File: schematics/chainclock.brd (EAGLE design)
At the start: 72 x 39.5 mm, 19 parts, among them SW1 ROTARTY_ENCODER

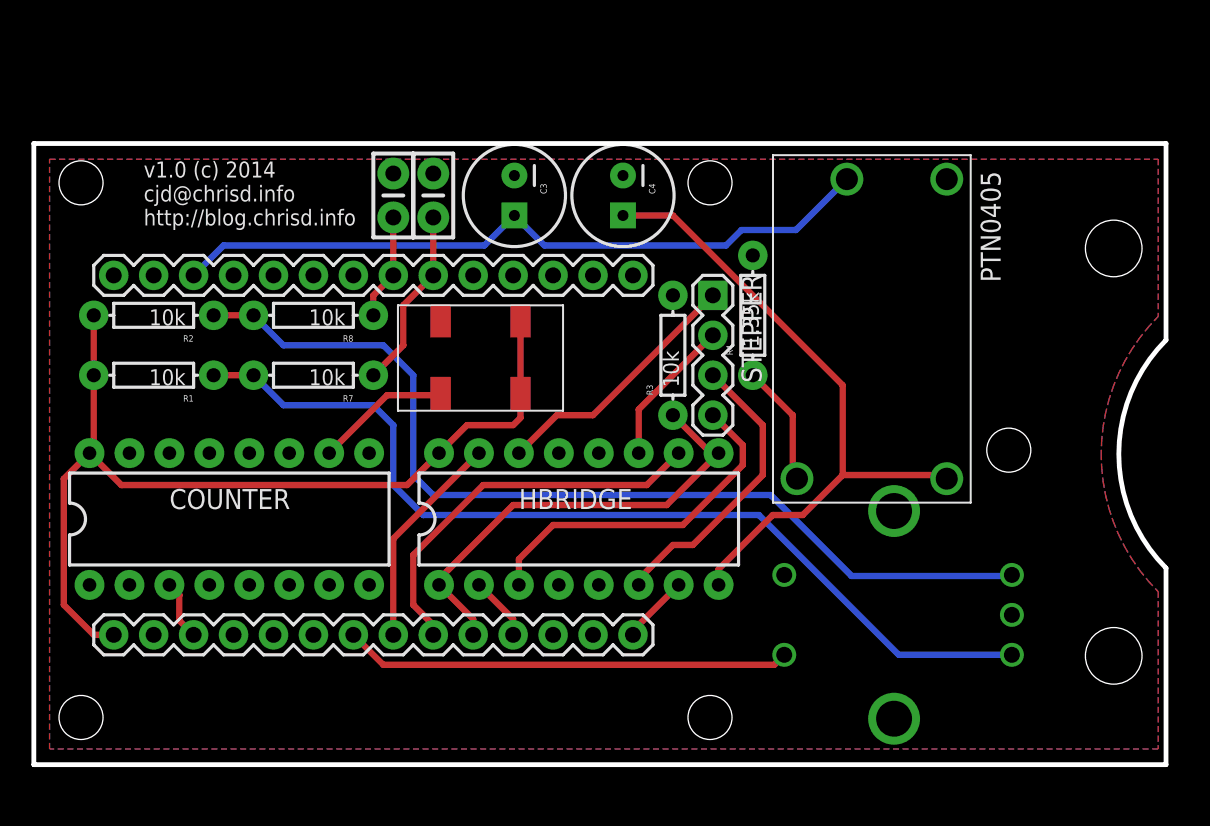
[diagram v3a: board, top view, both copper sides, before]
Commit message: Add voltage limiter for solar
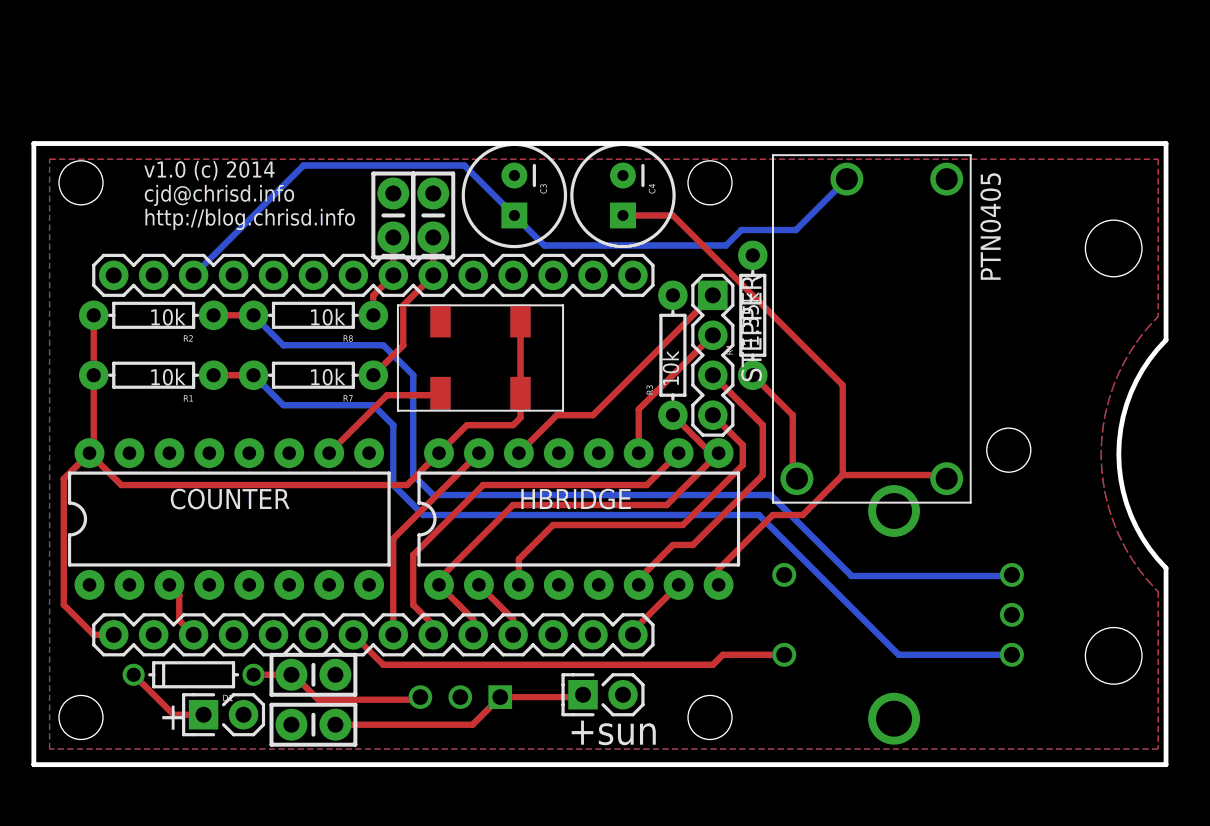
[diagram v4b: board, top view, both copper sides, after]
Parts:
- added C1: 10uf50v, SparkFun-Capacitors:CAP-PTH-SMALL-KIT
- added C2: 22uf6.3v, SparkFun-Capacitors:CAP-PTH-SMALL-KIT
- added D1: (no value), adafruit:DO-1N4148
- added JP1, JP2: M02POLAR, desjardins:MOLEX-1X2
- added U$1: V78-500, desjardins:V78-500
- moved C5 1.27 mm to (22.9, 34.9)
- moved C6 1.27 mm to (25.4, 34.9)
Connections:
- new net N$4: C2.1, D1.A, U$1.P$3
- new net VINSOLAR: C1.1, JP1.1, U$1.P$1
- new net VOUTSOLAR: D1.C, JP2.1
- net GND: now also C1.2, C2.2, JP1.2, JP2.2, U$1.P$2
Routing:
- net VINSOLAR: track 0.00 -> 16.5 mm
- net N$4: track 0.00 -> 11.3 mm
- net VOUTSOLAR: track 0.00 -> 5.50 mm
- net 3V31: track 45.7 -> 48.3 mm
- net RENCB: track 11.6 -> 10.3 mm
- net RENCA: track 6.75 -> 5.48 mm
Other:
- board text added: "+"
- board text added: "+sun"
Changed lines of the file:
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@@
 <setting verticaltext="up"/>
 </settings>
-<grid distance="0.5" unitdist="mm" unit="mm" style="lines" multiple="1" display="yes" altdistance="0.025" altunitdist="inch" altunit="inch"/>
+<grid distance="0.025" unitdist="inch" unit="inch" style="lines" multiple="1" display="yes" altdistance="0.025" altunitdist="inch" altunit="inch"/>
 <layers>
 <layer number="1" name="Top" color="4" fill="1" visible="yes" active="yes"/>
@@
 <wire x1="72" y1="12.5" x2="72" y2="0" width="0.3048" layer="20"/>
 <wire x1="0" y1="0" x2="72" y2="0" width="0.3048" layer="20"/>
+<text x="7.9375" y="2.2225" size="1.778" layer="21">+</text>
+<text x="33.9725" y="1.27" size="1.778" layer="21">+sun</text>
 </plain>
 <attributes>
@@
 <element name="U$3" library="desjardins" package="LOGO" value="" x="66.945" y="29.845" rot="MR270"/>
 <element name="SW1" library="SparkFun-Electromechanical" package="ROTARY_ENC_PLAIN" value="ROTARTY_ENCODER" x="54.705" y="9.525" rot="MR180"/>
-<element name="C5" library="SparkFun-Capacitors" package="CAP-PTH-SMALL-KIT" value=".01uf" x="22.86" y="36.195" rot="R90"/>
-<element name="C6" library="SparkFun-Capacitors" package="CAP-PTH-SMALL-KIT" value=".01uf" x="25.4" y="36.195" rot="R90"/>
+<element name="C5" library="SparkFun-Capacitors" package="CAP-PTH-SMALL-KIT" value=".01uf" x="22.86" y="34.925" rot="R90"/>
+<element name="C6" library="SparkFun-Capacitors" package="CAP-PTH-SMALL-KIT" value=".01uf" x="25.4" y="34.925" rot="R90"/>
 <element name="U$4" library="desjardins" package="SG3030JC" value="SG30XXJC" x="33.655" y="29.21" rot="R180"/>
 <element name="R1" library="SparkFun-Resistors" package="AXIAL-0.3EZ" value="10k" x="7.62" y="24.765" rot="R180"/>
@@
 <element name="R7" library="SparkFun-Resistors" package="AXIAL-0.3EZ" value="10k" x="17.78" y="24.765" rot="R180"/>
 <element name="R8" library="SparkFun-Resistors" package="AXIAL-0.3EZ" value="10k" x="17.78" y="28.575" rot="R180"/>
+<element name="U$1" library="desjardins" package="V78-500" value="V78-500" x="27.12" y="3.095" rot="R180"/>
+<element name="C1" library="SparkFun-Capacitors" package="CAP-PTH-SMALL-KIT" value="10uf50v" x="17.78" y="2.54" rot="R180"/>
+<element name="C2" library="SparkFun-Capacitors" package="CAP-PTH-SMALL-KIT" value="22uf6.3v" x="17.78" y="5.715"/>
+<element name="D1" library="adafruit" package="DO-1N4148" value="" x="10.16" y="5.715" rot="R180"/>
+<element name="JP1" library="desjardins" package="MOLEX-1X2" value="M02POLAR" x="34.925" y="4.445"/>
+<element name="JP2" library="desjardins" package="MOLEX-1X2" value="M02POLAR" x="10.795" y="3.175"/>
 </elements>
 <signals>
@@
 <vertex x="71.5" y="1"/>
 </polygon>
+<contactref element="U$1" pad="P$2"/>
+<contactref element="C1" pad="2"/>
+<contactref element="C2" pad="2"/>
+<contactref element="JP1" pad="2"/>
+<contactref element="JP2" pad="2"/>
 </signal>
 <signal name="3V30">
@@
 <contactref element="PTN0405" pad="2"/>
 <contactref element="C3" pad="1"/>
-<wire x1="10.16" y1="31.115" x2="12.065" y2="33.02" width="0.4064" layer="16"/>
-<wire x1="12.065" y1="33.02" x2="28.655" y2="33.02" width="0.4064" layer="16"/>
-<wire x1="28.655" y1="33.02" x2="30.56" y2="34.925" width="0.4064" layer="16"/>
 <wire x1="44.02" y1="33.02" x2="32.465" y2="33.02" width="0.4064" layer="16"/>
-<wire x1="32.465" y1="33.02" x2="30.56" y2="34.925" width="0.4064" layer="16"/>
 <wire x1="44.02" y1="33.02" x2="45" y2="34" width="0.4064" layer="16"/>
 <wire x1="45" y1="34" x2="48.468" y2="34" width="0.4064" layer="16"/>
 <wire x1="48.468" y1="34" x2="51.704" y2="37.236" width="0.4064" layer="16"/>
+<wire x1="32.465" y1="33.02" x2="30.56" y2="34.925" width="0.4064" layer="16"/>
+<wire x1="10.16" y1="31.115" x2="17.145" y2="38.1" width="0.4064" layer="16"/>
+<wire x1="17.145" y1="38.1" x2="27.385" y2="38.1" width="0.4064" layer="16"/>
+<wire x1="27.385" y1="38.1" x2="30.56" y2="34.925" width="0.4064" layer="16"/>
 </signal>
 <signal name="3V32">
@@
 <contactref element="SW1" pad="SW+"/>
 <contactref element="ARDUNOFIO" pad="7"/>
-<wire x1="47.085" y1="6.35" x2="22.225" y2="6.35" width="0.4064" layer="1"/>
 <wire x1="22.225" y1="6.35" x2="20.32" y2="8.255" width="0.4064" layer="1"/>
-<wire x1="47.085" y1="6.35" x2="47.72" y2="6.985" width="0.4064" layer="1"/>
+<wire x1="22.225" y1="6.35" x2="43.18" y2="6.35" width="0.4064" layer="1"/>
+<wire x1="43.815" y1="6.985" x2="47.72" y2="6.985" width="0.4064" layer="1"/>
+<wire x1="43.18" y1="6.35" x2="43.815" y2="6.985" width="0.4064" layer="1"/>
 </signal>
 <signal name="RENCB">
@@
 <wire x1="23.495" y1="26.67" x2="23.495" y2="29.21" width="0.4064" layer="1"/>
 <wire x1="23.495" y1="29.21" x2="25.4" y2="31.115" width="0.4064" layer="1"/>
-<wire x1="25.4" y1="34.798" x2="25.4" y2="31.115" width="0.4064" layer="1"/>
+<wire x1="25.4" y1="33.528" x2="25.4" y2="31.115" width="0.4064" layer="1"/>
 <wire x1="23.495" y1="26.67" x2="21.59" y2="24.765" width="0.4064" layer="1"/>
 </signal>
@@
 <wire x1="21.59" y1="28.575" x2="21.59" y2="29.845" width="0.4064" layer="1"/>
 <wire x1="21.59" y1="29.845" x2="22.86" y2="31.115" width="0.4064" layer="1"/>
-<wire x1="22.86" y1="34.798" x2="22.86" y2="31.115" width="0.4064" layer="1"/>
+<wire x1="22.86" y1="33.528" x2="22.86" y2="31.115" width="0.4064" layer="1"/>
 </signal>
 <signal name="RTC">
@@
 <wire x1="22.463" y1="23.495" x2="18.78" y2="19.812" width="0.4064" layer="1"/>
 </signal>
+<signal name="VOUTSOLAR">
+<contactref element="D1" pad="C"/>
+<contactref element="JP2" pad="1"/>
+<wire x1="6.35" y1="5.715" x2="8.89" y2="3.175" width="0.4064" layer="1"/>
+<wire x1="8.89" y1="3.175" x2="10.795" y2="3.175" width="0.4064" layer="1"/>
+</signal>
+<signal name="VINSOLAR">
+<contactref element="U$1" pad="P$1"/>
+<contactref element="C1" pad="1"/>
+<contactref element="JP1" pad="1"/>
+<wire x1="19.177" y1="2.54" x2="27.905" y2="2.54" width="0.4064" layer="1"/>
+<wire x1="27.905" y1="2.54" x2="29.66" y2="4.295" width="0.4064" layer="1"/>
+<wire x1="29.66" y1="4.295" x2="34.775" y2="4.295" width="0.4064" layer="1"/>
+<wire x1="34.775" y1="4.295" x2="34.925" y2="4.445" width="0.4064" layer="1"/>
+</signal>
+<signal name="N$4">
+<contactref element="U$1" pad="P$3"/>
+<contactref element="D1" pad="A"/>
+<contactref element="C2" pad="1"/>
+<wire x1="13.97" y1="5.715" x2="16.383" y2="5.715" width="0.4064" layer="1"/>
+<wire x1="16.383" y1="5.715" x2="16.51" y2="5.715" width="0.4064" layer="1"/>
+<wire x1="16.51" y1="5.715" x2="18.0975" y2="4.1275" width="0.4064" layer="1"/>
+<wire x1="18.0975" y1="4.1275" x2="24.4125" y2="4.1275" width="0.4064" layer="1"/>
+<wire x1="24.4125" y1="4.1275" x2="24.58" y2="4.295" width="0.4064" layer="1"/>
+</signal>
 </signals>

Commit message: Updates to the counter
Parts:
- renumbered U$4 to SG3040JC
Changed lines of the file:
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@@
 <element name="C5" library="SparkFun-Capacitors" package="CAP-PTH-SMALL-KIT" value=".01uf" x="22.86" y="34.925" rot="R90"/>
 <element name="C6" library="SparkFun-Capacitors" package="CAP-PTH-SMALL-KIT" value=".01uf" x="25.4" y="34.925" rot="R90"/>
-<element name="U$4" library="desjardins" package="SG3030JC" value="SG30XXJC" x="33.655" y="29.21" rot="R180"/>
+<element name="SG3040JC" library="desjardins" package="SG3030JC" value="SG30XXJC" x="33.655" y="29.21" rot="R180"/>
 <element name="R1" library="SparkFun-Resistors" package="AXIAL-0.3EZ" value="10k" x="7.62" y="24.765" rot="R180"/>
 <element name="R2" library="SparkFun-Resistors" package="AXIAL-0.3EZ" value="10k" x="7.62" y="28.575" rot="R180"/>
@@
 <contactref element="C5" pad="2"/>
 <contactref element="SW1" pad="SW-"/>
-<contactref element="U$4" pad="2"/>
-<contactref element="U$4" pad="2"/>
+<contactref element="SG3040JC" pad="2"/>
+<contactref element="SG3040JC" pad="2"/>
 <polygon width="0.4064" layer="16">
 <vertex x="1" y="1"/>
@@
 <contactref element="COUNTER" pad="16"/>
 <contactref element="HBRIDGE" pad="16"/>
-<contactref element="U$4" pad="4"/>
-<contactref element="U$4" pad="1"/>
+<contactref element="SG3040JC" pad="4"/>
+<contactref element="SG3040JC" pad="1"/>
 <contactref element="R2" pad="P$2"/>
 <contactref element="R1" pad="P$2"/>
@@
 <signal name="RTC">
 <contactref element="COUNTER" pad="10"/>
-<contactref element="U$4" pad="3"/>
+<contactref element="SG3040JC" pad="3"/>
 <wire x1="22.463" y1="23.495" x2="25.75" y2="23.495" width="0.4064" layer="1"/>
 <wire x1="25.75" y1="23.495" x2="25.865" y2="23.61" width="0.4064" layer="1"/>

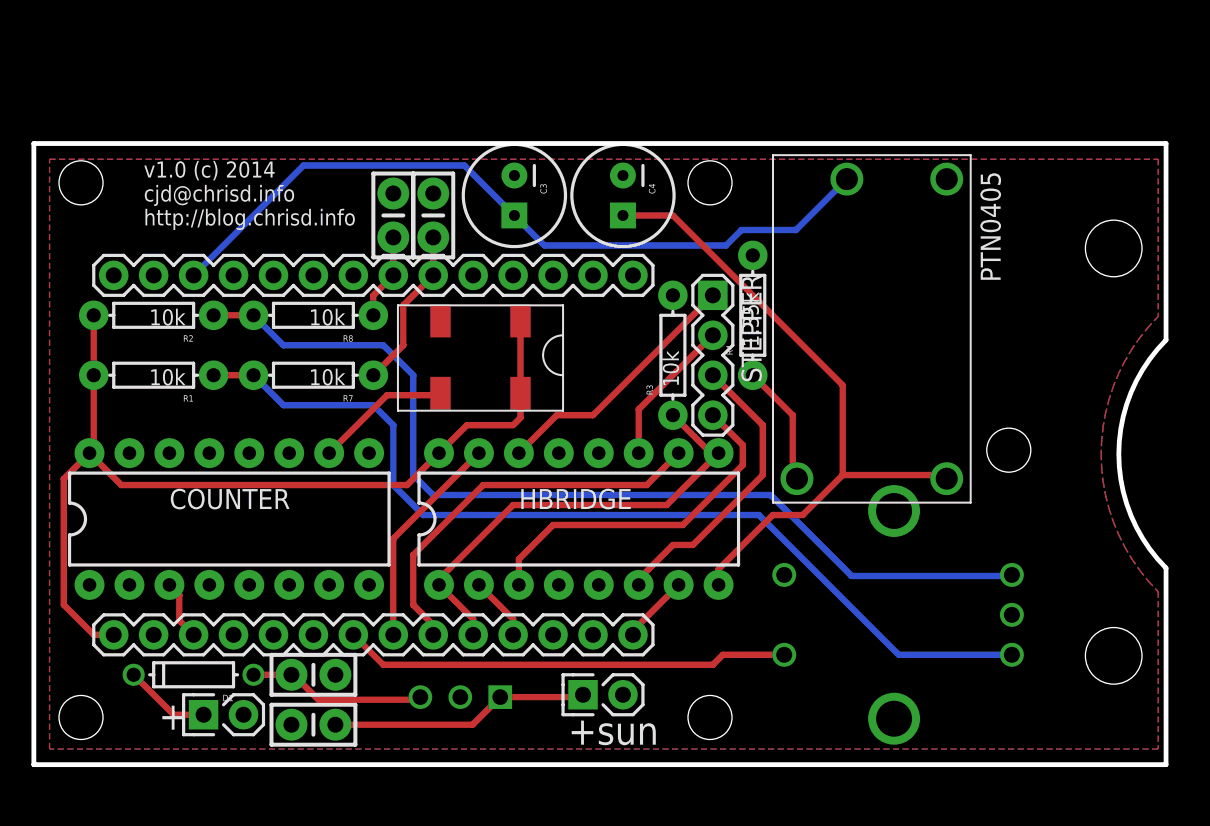
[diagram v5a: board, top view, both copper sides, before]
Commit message: Updated to use 2 4060 and...
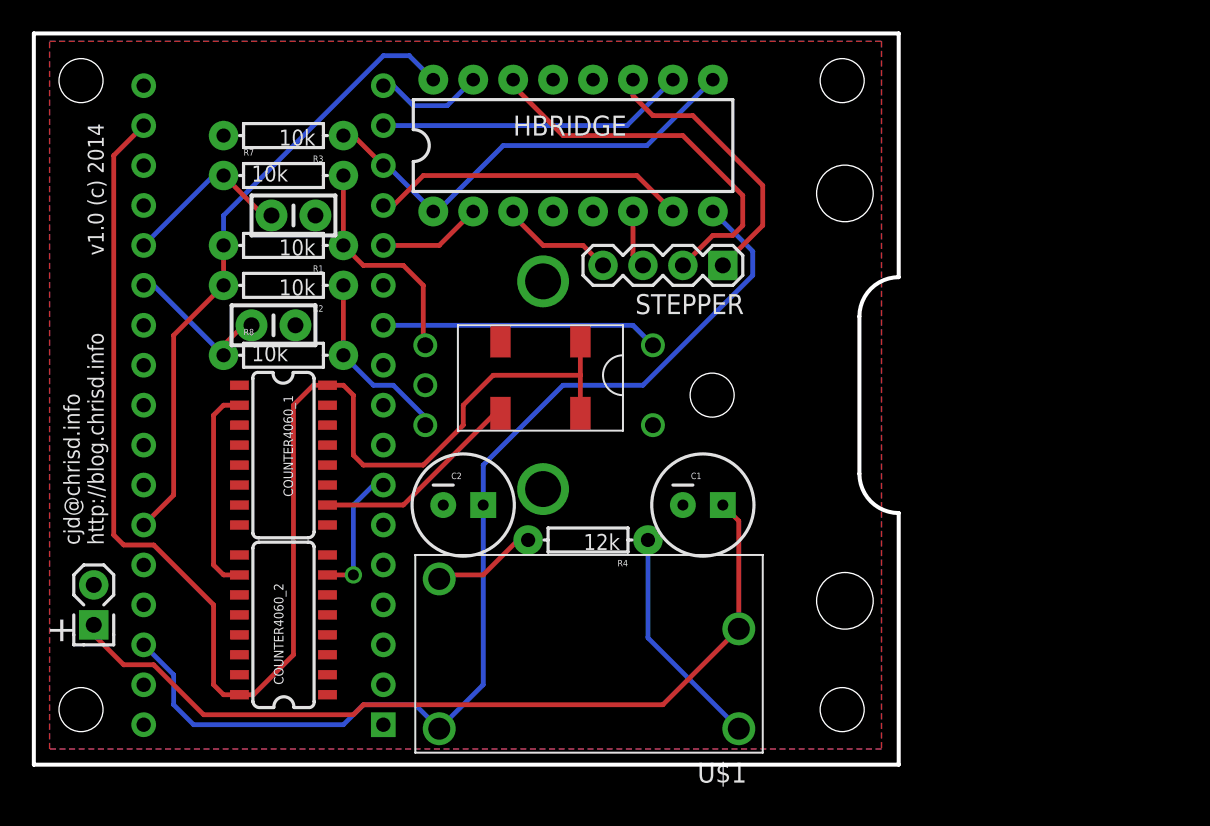
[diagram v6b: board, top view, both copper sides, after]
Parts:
- removed ARDUNOFIO: ARDUINOFIO, desjardins:ARDUINOFIO
- removed C3, C4: (no value), SparkFun-Passives:CPOL-RADIAL-100UF-25V
- removed COUNTER: 4060, desjardins:DIL16-KIT
- removed D1: (no value), adafruit:DO-1N4148
- removed JP2: M02POLAR, desjardins:MOLEX-1X2
- removed PTN0405: PTN0405C, desjardins:EUU4
- added COUNTER4060_1, COUNTER4060_2: 4060SOIC16, desjardins:SO016
- added U$4: ARDUINO_PRO_MICRO, ChrisD:ARDUINO_PRO_MICRO
- C1: value 10uf50v -> (none); device SparkFun-Capacitors:CAP-PTH-SMALL-KIT -> SparkFun-Capacitors:CPOL-RADIAL-100UF-25V
- C2: value 22uf6.3v -> (none); device SparkFun-Capacitors:CAP-PTH-SMALL-KIT -> SparkFun-Capacitors:CPOL-RADIAL-100UF-25V
- R4: value 1.35k -> 12k
- U$1: value V78-500 -> PTN0405C; device desjardins:V78-500 -> desjardins:EUU4
- moved JP1 31.4 mm to (3.81, 8.89), turned to 90 degrees
- moved C1 28.4 mm to (42.5, 16.5), turned to 0 degrees
- moved R3 28.4 mm to (15.9, 40.0), turned to 180 degrees
- moved SW1 26.7 mm to (32.4, 24.1), turned to 0 degrees
- moved HBRIDGE 23.8 mm to (34.3, 39.4)
- moved U$1 21.8 mm to (46.4, 13.3)
- moved U$3 17.9 mm to (49.4, 33.3)
- moved R4 17.7 mm to (35.2, 14.3), turned to 180 degrees
- moved U$2 17.4 mm to (64.4, 23.5)
- moved C2 14.4 mm to (27.3, 16.5)
- moved R7 12.8 mm to (15.9, 37.5), turned to 0 degrees
- moved R1 11.7 mm to (15.9, 33.0)
- moved C5 10.3 mm to (15.2, 27.9), turned to 0 degrees
- moved C6 8.89 mm to (16.5, 34.9), turned to 0 degrees
- moved R2 8.47 mm to (15.9, 30.5)
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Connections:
- removed net 3V31: ARDUNOFIO.26, C3.1, PTN0405.2
- removed net 3V32: ARDUNOFIO.1, COUNTER.16, HBRIDGE.16, R1.P$2, R2.P$2, SG3040JC.1, SG3040JC.4
- removed net N$3: PTN0405.3, R4.P$1
- removed net N$4: C2.1, D1.A, U$1.P$3
- removed net Q14: ARDUNOFIO.3, COUNTER.3
- removed net VDD12: C4.1, HBRIDGE.8, PTN0405.4
- removed net VINSOLAR: C1.1, JP1.1, U$1.P$1
- removed net VOUTSOLAR: D1.C, JP2.1
- new net 3V3: COUNTER4060_1.16, COUNTER4060_2.16, SG3040JC.1, SG3040JC.4, U$4.P19
- new net 5VREG: HBRIDGE.16, R1.P$2, R2.P$2, U$4.P29
- new net CLOCKIN: COUNTER4060_2.7, U$4.P7
- new net GND0: U$4.P6
- new net GND1: U$4.P31
- new net N$1: R4.P$1, U$1.1
- new net Q13: COUNTER4060_1.2, COUNTER4060_2.10
- new net REF: U$4.P20
- new net VBATT: C1.1, JP1.1, U$1.2
- new net VIN: C2.1, HBRIDGE.8, U$1.4, U$4.P32
- new net VOADJ: R4.P$2, U$1.3
- net 1A: now also U$4.P13; no longer ARDUNOFIO.11
- net 2A: now also U$4.P14; no longer ARDUNOFIO.14
- net 3A: now also U$4.P16; no longer ARDUNOFIO.9
- net 3Y: now also STEPPER.1; no longer STEPPER.2
- net 4A: now also U$4.P17; no longer ARDUNOFIO.8
- net 4Y: now also STEPPER.2; no longer STEPPER.1
- net EN: now also U$4.P15; no longer ARDUNOFIO.10
- net GND: now also COUNTER4060_1.12, COUNTER4060_1.8, COUNTER4060_2.12, COUNTER4060_2.8; no longer ARDUNOFIO.2, ARDUNOFIO.28, C3.2, C4.2, COUNTER.12, COUNTER.8, JP2.2, PTN0405.1, R4.P$2, U$1.P$2
- net RENBTN: now also U$4.P11; no longer ARDUNOFIO.7
- net RENCA: now also U$4.P23; no longer ARDUNOFIO.21
- net RENCB: now also U$4.P22; no longer ARDUNOFIO.20
- net RTC: now also COUNTER4060_1.10; no longer COUNTER.10
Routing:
- net 3V3: track 0.00 -> 93.2 mm
- net VIN: track 0.00 -> 68.4 mm
- net 3V32: track 59.3 -> 0.00 mm
- net VBATT: track 0.00 -> 54.3 mm
- net N$5: track 61.4 -> 11.8 mm
- net 3V31: track 48.3 -> 0.00 mm
- net N$2: track 60.4 -> 14.4 mm
- net VDD12: track 42.2 -> 0.00 mm
- net 5VREG: track 0.00 -> 40.0 mm
- net VINSOLAR: track 16.5 -> 0.00 mm
- net 2A: track 4.38 -> 20.2 mm
- net 1Y: track 22.3 -> 7.28 mm
- net 2Y: track 18.7 -> 3.69 mm
- net N$1: track 0.00 -> 14.4 mm
- net Q13: track 0.00 -> 13.3 mm
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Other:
- board size 72 x 39.5 mm -> 55 x 46.5 mm
- board text added: "cjd@chrisd.info http://blog.chrisd.info"
- board text added: "v1.0 (c) 2014"
- board text removed: "+sun"
- board text removed: "v1.0 (c) 2014 cjd@chrisd.info http://blog.chrisd.info"
